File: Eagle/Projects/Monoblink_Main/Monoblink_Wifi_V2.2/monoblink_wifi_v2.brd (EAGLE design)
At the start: 26 x 35 mm, 25 parts

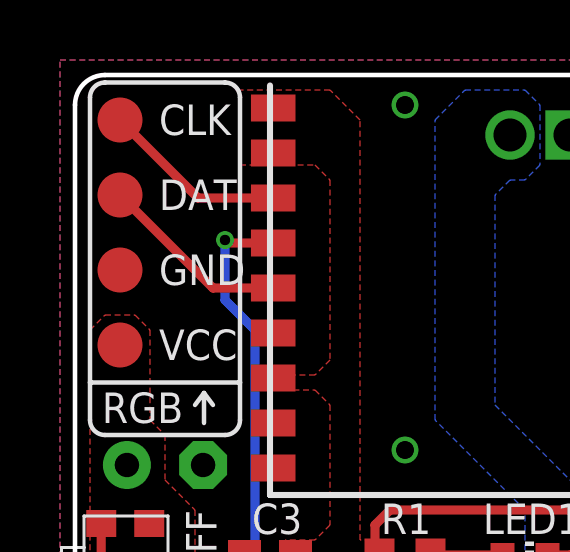
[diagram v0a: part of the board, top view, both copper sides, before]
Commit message: dio commander
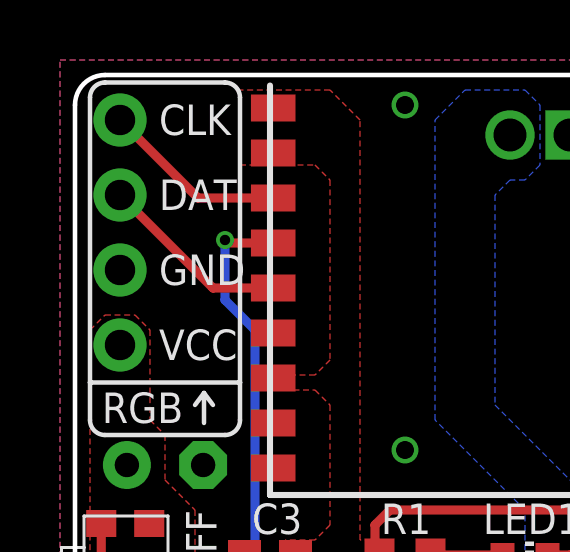
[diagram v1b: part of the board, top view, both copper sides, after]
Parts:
- CLK, DAT, GND, VCC: value TESTPAD_PROG -> TESTPAD_PROGSPRING_PIN; device monoblink_wifi:TP1.5MM -> monoblink_wifi:MATRIX_CONN
